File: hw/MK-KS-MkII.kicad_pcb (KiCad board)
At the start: 2 copper layers, 104.1 x 78.7 mm, 57 parts, among them J2 LOOP PWR, J3 UART Data, J4 MuKOB IF, J5 KEY-PADDLE, Q3 G01N20LE, Q4 2N3904, SW1 CLOSER, SW2 KEY/DOT, SW3 DASH, U1 FT234XF_USB_UART_Module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

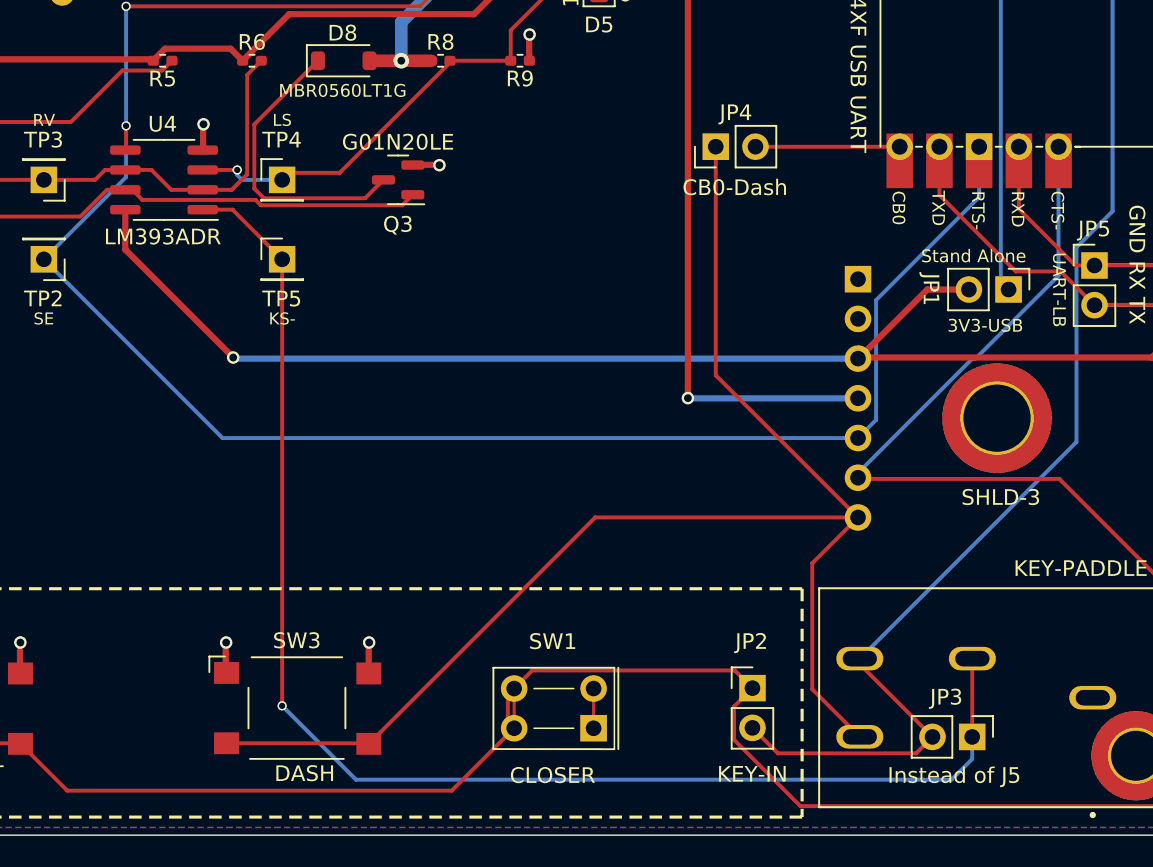
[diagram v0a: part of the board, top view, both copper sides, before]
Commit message: KSInf-MkIII: New  JA: Add terminal block
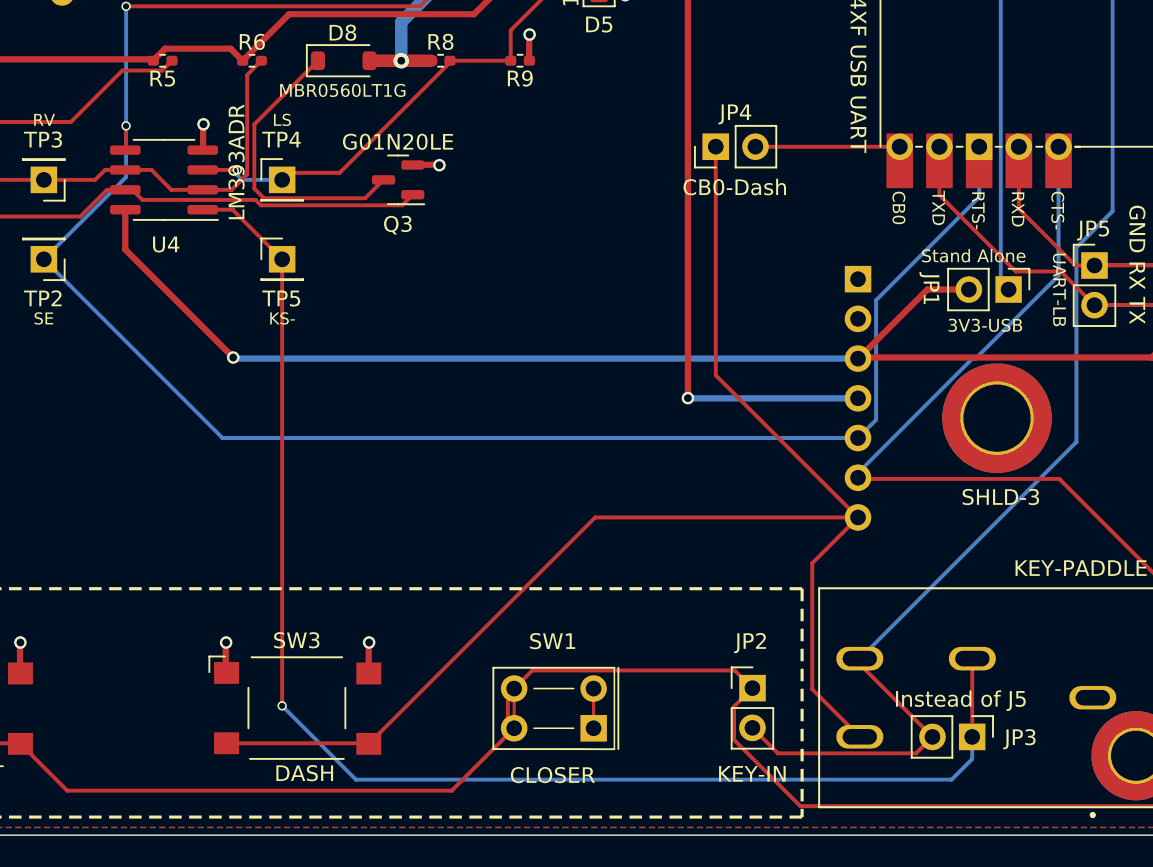
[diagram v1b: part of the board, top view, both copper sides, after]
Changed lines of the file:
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@@
     (title "MuKOB-Key & Sounder Interface, MKOB4 USB Interface")
     (date "2024-01-12")
-    (rev "1.0")
+    (rev "1.0 B")
     (company "Silky Design AES")
     (comment 1 "Copyright AESilky 2023-24")
@@
     (property "ki_keywords" "Jumper SPST")
     (attr through_hole)
-    (fp_text reference "JP3" (at -2.534 1.646) (layer "F.SilkS")
+    (fp_text reference "JP3" (at 0.056 -3.11) (layer "F.SilkS")
         (effects (font (size 1 1) (thickness 0.15)))
     )
@@
         (effects (font (size 1 1) (thickness 0.15)))
     )
-    (fp_text user "Instead of J5" (at 2.472 1.147 unlocked) (layer "F.SilkS")
+    (fp_text user "Instead of J5" (at -2.397 0.731 unlocked) (layer "F.SilkS")
         (effects (font (size 1 1) (thickness 0.15)))
     )
@@
     (property "Status" "Active")
     (attr smd)
-    (fp_text reference "U4" (at 0.0904 3.556) (layer "F.SilkS")
+    (fp_text reference "U4" (at -0.1176 -4.1612) (layer "F.SilkS")
         (effects (font (size 1 1) (thickness 0.15)))
     )
-    (fp_text value "LM393ADR" (at 0.0904 -3.6576 180) (layer "F.SilkS")
+    (fp_text value "LM393ADR" (at -4.6736 1.1048 270) (layer "F.SilkS")
         (effects (font (size 1 1) (thickness 0.15)))
     )
@@
     )
   )
-  (gr_text "OPa2\nKOB Debug Power\nDO NOT CONNECT\nw/Loop Powered" (at 73.025 135.1788) (layer "B.SilkS")
+  (gr_text "OPa2\nKOB Debug Power\nDO NOT CONNECT\nw/Loop Powered" (at 60.522 126.944 -90) (layer "B.SilkS")
     (effects (font (size 0.8128 0.8128) (thickness 0.1016)) (justify left bottom mirror))
   )
-  (gr_text "JP1\nMKOB Interface Power\nDO NOT CONNECT\nfor μKOB\n" (at 187.665 149.009) (layer "B.SilkS")
+  (gr_text "JP1\nMKOB Interface Power\nDO NOT CONNECT\nfor μKOB\n" (at 130.454 132.497) (layer "B.SilkS")
     (effects (font (size 0.8128 0.8128) (thickness 0.1016)) (justify left mirror))
   )
@@
     (pts (xy 56.1594 93.5228) (xy 160.2994 93.5228))
     (height -14.732)
-    (gr_text "104.1400 mm" (at 108.2294 77.6408) (layer "User.2")
+    (gr_text "4.1000 in" (at 108.2294 77.6408) (layer "User.2")
       (effects (font (size 1 1) (thickness 0.15)))
     )
@@
     (pts (xy 61.2394 98.6028) (xy 155.2194 98.6028))
     (height -15.24)
-    (gr_text "93.9800 mm" (at 108.2294 82.2128) (layer "User.2")
+    (gr_text "3.7000 in" (at 108.2294 82.2128) (layer "User.2")
       (effects (font (size 1 1) (thickness 0.15)))
     )
@@
     (pts (xy 61.2394 98.6028) (xy 137.4394 98.6028))
     (height -10.16)
-    (gr_text "76.2000 mm" (at 99.3394 87.2928) (layer "User.2")
+    (gr_text "3.0000 in" (at 99.3394 87.2928) (layer "User.2")
       (effects (font (size 1 1) (thickness 0.15)))
     )
@@
     (pts (xy 61.2394 98.6028) (xy 61.2394 136.7028))
     (height 10.159999)
-    (gr_text "38.1000 mm" (at 49.929401 117.6528 90) (layer "User.2")
+    (gr_text "1.5000 in" (at 49.929401 117.6528 90) (layer "User.2")
       (effects (font (size 1 1) (thickness 0.15)))
     )
@@
     (pts (xy 61.2394 98.6028) (xy 61.2394 167.1828))
     (height 15.239999)
-    (gr_text "68.5800 mm" (at 44.849401 132.8928 90) (layer "User.2")
+    (gr_text "2.7000 in" (at 44.849401 132.8928 90) (layer "User.2")
       (effects (font (size 1 1) (thickness 0.15)))
     )
@@
     (pts (xy 56.1594 93.5228) (xy 56.1594 172.2628))
     (height 15.24)
-    (gr_text "78.7400 mm" (at 39.7694 132.8928 90) (layer "User.2")
+    (gr_text "3.1000 in" (at 39.7694 132.8928 90) (layer "User.2")
       (effects (font (size 1 1) (thickness 0.15)))
     )
